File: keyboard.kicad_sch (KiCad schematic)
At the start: 1 part, among them U11 MCP3208

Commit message: кнопки
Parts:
- added SW1, SW2: SW_Push, Button_Switch_THT:SW_PUSH_6mm_H9.5mm, symbol Switch:SW_Push
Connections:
- net RFGND: now also SW1.1, SW2.1
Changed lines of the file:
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@@
+	(wire
+		(pts
+			(xy 74.93 71.12) (xy 81.28 71.12)
+		)
+		(stroke
+			(width 0)
+			(type default)
+		)
+	)
 	(wire
 		(pts
@@
 		(pts
 			(xy 266.7 113.03) (xy 266.7 121.92)
+		)
+		(stroke
+			(width 0)
+			(type default)
+		)
+	)
+	(wire
+		(pts
+			(xy 74.93 88.9) (xy 81.28 88.9)
 		)
 		(stroke
@@
 		)
 	)
+	(label "RFGND"
+		(at 74.93 88.9 180)
+		(effects
+			(font
+				(size 1.27 1.27)
+			)
+			(justify right bottom)
+		)
+	)
 	(label "AVDD_3P3"
 		(at 245.11 78.74 180)
+		(effects
+			(font
+				(size 1.27 1.27)
+			)
+			(justify right bottom)
+		)
+	)
+	(label "RFGND"
+		(at 74.93 71.12 180)
 		(effects
 			(font
@@
 			)
 		)
+	)
+	(symbol
+		(lib_id "Switch:SW_Push")
+		(at 86.36 88.9 0)
+		(unit 1)
+		(body_style 1)
+		(exclude_from_sim no)
+		(in_bom yes)
+		(on_board yes)
+		(in_pos_files yes)
+		(dnp no)
+		(fields_autoplaced yes)
+		(property "Reference" "SW2"
+			(at 86.36 81.28 0)
+			(show_name no)
+			(do_not_autoplace no)
+			(effects
+				(font
+					(size 1.27 1.27)
+				)
+			)
+		)
+		(property "Value" "SW_Push"
+			(at 86.36 83.82 0)
+			(show_name no)
+			(do_not_autoplace no)
+			(effects
+				(font
+					(size 1.27 1.27)
+				)
+			)
+		)
+		(property "Footprint" "Button_Switch_THT:SW_PUSH_6mm_H9.5mm"
+			(at 86.36 83.82 0)
+			(hide yes)
+			(show_name no)
+			(do_not_autoplace no)
+			(effects
+				(font
+					(size 1.27 1.27)
+				)
+			)
+		)
+		(property "Datasheet" ""
+			(at 86.36 83.82 0)
+			(hide yes)
+			(show_name no)
+			(do_not_autoplace no)
+			(effects
+				(font
+					(size 1.27 1.27)
+				)
+			)
+		)
+		(property "Description" "Push button switch, generic, two pins"
+			(at 86.36 88.9 0)
+			(hide yes)
+			(show_name no)
+			(do_not_autoplace no)
+			(effects
+				(font
+					(size 1.27 1.27)
+				)
+			)
+		)
+		(pin "1"
+		)
+		(pin "2"
+		)
+		(instances
+			(project "testprj"
+				(path "/423c1216-1c87-4878-aa19-5de0f026118b/ea99654f-353c-4d51-908f-8daad505ae1a"
+					(reference "SW2")
+					(unit 1)
+				)
+			)
+		)
+	)
+	(symbol
+		(lib_id "Switch:SW_Push")
+		(at 86.36 71.12 0)
+		(unit 1)
+		(body_style 1)
+		(exclude_from_sim no)
+		(in_bom yes)
+		(on_board yes)
+		(in_pos_files yes)
+		(dnp no)
+		(fields_autoplaced yes)
+		(property "Reference" "SW1"
+			(at 86.36 63.5 0)
+			(show_name no)
+			(do_not_autoplace no)
+			(effects
+				(font
+					(size 1.27 1.27)
+				)
+			)
+		)
+		(property "Value" "SW_Push"
+			(at 86.36 66.04 0)
+			(show_name no)
+			(do_not_autoplace no)
+			(effects
+				(font
+					(size 1.27 1.27)
+				)
+			)
+		)
+		(property "Footprint" "Button_Switch_THT:SW_PUSH_6mm_H9.5mm"
+			(at 86.36 66.04 0)
+			(hide yes)
+			(show_name no)
+			(do_not_autoplace no)
+			(effects
+				(font
+					(size 1.27 1.27)
+				)
+			)
+		)
+		(property "Datasheet" ""
+			(at 86.36 66.04 0)
+			(hide yes)
+			(show_name no)
+			(do_not_autoplace no)
+			(effects
+				(font
+					(size 1.27 1.27)
+				)
+			)
+		)
+		(property "Description" "Push button switch, generic, two pins"
+			(at 86.36 71.12 0)
+			(hide yes)
+			(show_name no)
+			(do_not_autoplace no)
+			(effects
+				(font
+					(size 1.27 1.27)
+				)
+			)
+		)
+		(pin "1"
+		)
+		(pin "2"
+		)
+		(instances
+			(project "testprj"
+				(path "/423c1216-1c87-4878-aa19-5de0f026118b/ea99654f-353c-4d51-908f-8daad505ae1a"
+					(reference "SW1")
+					(unit 1)
+				)
+			)
+		)

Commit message: кнопки
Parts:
- added C34, C35, C36, C37, C38: 8200 pF, Capacitor_SMD:C_0805_2012Metric_Pad1.18x1.45mm_HandSolder, symbol Device:C
- added R14, R18, R22, R26, R30: 6K8 F, Resistor_SMD:R_0805_2012Metric_Pad1.20x1.40mm_HandSolder, symbol Device:R
- added R15, R19, R23, R27, R31: 2K2 F, Resistor_SMD:R_0805_2012Metric_Pad1.20x1.40mm_HandSolder, symbol Device:R
- added R16, R20, R24, R28, R32: 4K7 F, Resistor_SMD:R_0805_2012Metric_Pad1.20x1.40mm_HandSolder, symbol Device:R
- added R17, R21, R25, R29, R33: 13K F, Resistor_SMD:R_0805_2012Metric_Pad1.20x1.40mm_HandSolder, symbol Device:R
- added SW10, SW11, SW12, SW13, SW14, SW15, SW16, SW17, SW18, SW19, SW20, SW3, SW4, SW5, SW6, SW7, SW8, SW9: SW_Push, Button_Switch_THT:SW_PUSH_6mm_H9.5mm, symbol Switch:SW_Push
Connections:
- net AVDD_3P3: now also R14.2, R18.2, R22.2, R26.2, R30.2
- net RFGND: now also C34.2, C35.2, C36.2, C37.2, C38.2, SW10.1, SW11.1, SW12.1, SW13.1, SW14.1, SW15.1, SW16.1, SW17.1, SW18.1, SW19.1, SW20.1, SW3.1, SW4.1, SW5.1, SW6.1, SW7.1, SW8.1, SW9.1
- net at SW2.2: now also R15.1, R16.2
- net KI0: now reaches SW1.2
- net KI0: now also U11.1 (CH0), C36.1, R14.1, R15.2
- net KI1: now reaches U11.2 (CH1)
- net KI1: now also C34.1, R18.1, R19.2, SW5.2
- net KI2: now reaches U11.3 (CH2)
- net KI2: now also C35.1, R22.1, R23.2, SW9.2
- net KI3: now reaches U11.4 (CH3)
- net KI3: now also C37.1, R26.1, R27.2, SW13.2
- net KI4: now reaches U11.5 (CH4)
- net KI4: now also C38.1, R30.1, R31.2, SW17.2
- new net: R19.1, R20.2, SW6.2
- new net: R32.1, R33.2, SW19.2
- new net: R31.1, R32.2, SW18.2
- new net: R23.1, R24.2, SW10.2
- new net: R25.1, SW12.2
- new net: R17.1, SW4.2
- new net: R16.1, R17.2, SW3.2
- new net: R28.1, R29.2, SW15.2
- new net: R33.1, SW20.2
- new net: R20.1, R21.2, SW7.2
- new net: R21.1, SW8.2
- new net: R24.1, R25.2, SW11.2
- new net: R27.1, R28.2, SW14.2
- new net: R29.1, SW16.2
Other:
- moved on the sheet: SW1, SW2

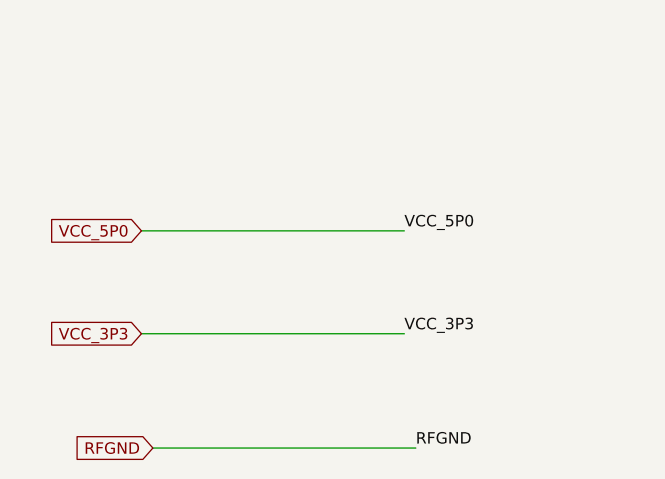
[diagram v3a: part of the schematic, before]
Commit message: add lcd backlight chip
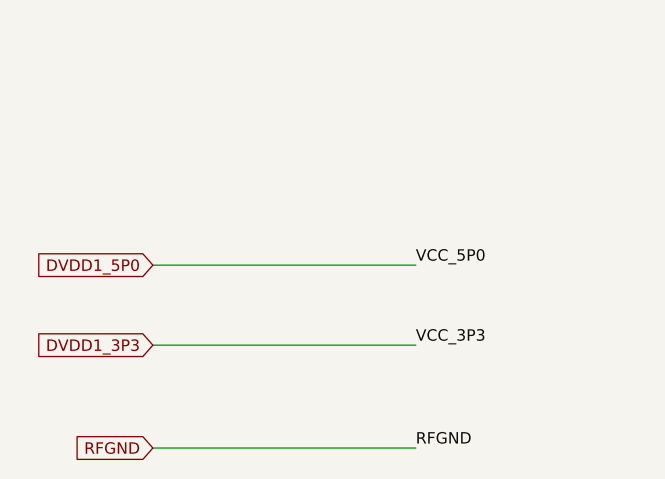
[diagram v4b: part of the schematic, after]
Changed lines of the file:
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@@
-	(wire
-		(pts
-			(xy 73.66 220.98) (xy 102.87 220.98)
-		)
-		(stroke
-			(width 0)
-			(type default)
-		)
-	)
 	(wire
 		(pts
@@
 	(wire
 		(pts
+			(xy 74.93 224.79) (xy 104.14 224.79)
+		)
+		(stroke
+			(width 0)
+			(type default)
+		)
+	)
+	(wire
+		(pts
 			(xy 105.41 60.96) (xy 105.41 62.23)
 		)
@@
 	(wire
 		(pts
-			(xy 73.66 232.41) (xy 102.87 232.41)
-		)
-		(stroke
-			(width 0)
-			(type default)
-		)
-	)
-	(wire
-		(pts
 			(xy 215.9 137.16) (xy 212.09 137.16)
 		)
@@
 		(pts
 			(xy 127 76.2) (xy 129.54 76.2)
+		)
+		(stroke
+			(width 0)
+			(type default)
+		)
+	)
+	(wire
+		(pts
+			(xy 74.93 233.68) (xy 104.14 233.68)
 		)
 		(stroke
@@
 		)
 	)
+	(label "VCC_3P3"
+		(at 104.14 233.68 0)
+		(effects
+			(font
+				(size 1.27 1.27)
+			)
+			(justify left bottom)
+		)
+	)
 	(label "KI3"
 		(at 209.55 97.79 180)
@@
 		)
 	)
-	(label "VCC_5P0"
-		(at 102.87 220.98 0)
-		(effects
-			(font
-				(size 1.27 1.27)
-			)
-			(justify left bottom)
-		)
-	)
 	(label "KI0"
 		(at 209.55 90.17 180)
@@
 		)
 	)
-	(label "VCC_3P3"
-		(at 102.87 232.41 0)
-		(effects
-			(font
-				(size 1.27 1.27)
-			)
-			(justify left bottom)
-		)
-	)
 	(label "KI3"
 		(at 115.57 124.46 0)
@@
 		)
 	)
+	(label "VCC_5P0"
+		(at 104.14 224.79 0)
+		(effects
+			(font
+				(size 1.27 1.27)
+			)
+			(justify left bottom)
+		)
+	)
 	(label "AVDD_3P3"
 		(at 175.26 53.34 180)
@@
 		)
 	)
-	(global_label "VCC_5P0"
+	(global_label "DVDD1_5P0"
 		(shape input)
-		(at 73.66 220.98 180)
+		(at 74.93 224.79 180)
 		(fields_autoplaced yes)
 		(effects
@@
 		)
 		(property "Intersheetrefs" "${INTERSHEET_REFS}"
-			(at 62.3896 220.98 0)
+			(at 61.1801 224.79 0)
 			(hide yes)
 			(show_name no)
@@
 		)
 	)
-	(global_label "VCC_3P3"
+	(global_label "DVDD1_3P3"
 		(shape input)
-		(at 73.66 232.41 180)
+		(at 74.93 233.68 180)
 		(fields_autoplaced yes)
 		(effects
@@
 		)
 		(property "Intersheetrefs" "${INTERSHEET_REFS}"
-			(at 62.3896 232.41 0)
+			(at 61.1801 233.68 0)
 			(hide yes)
 			(show_name no)
